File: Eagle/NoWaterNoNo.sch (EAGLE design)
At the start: 14 parts, among them U2 TINY85-20-DIP

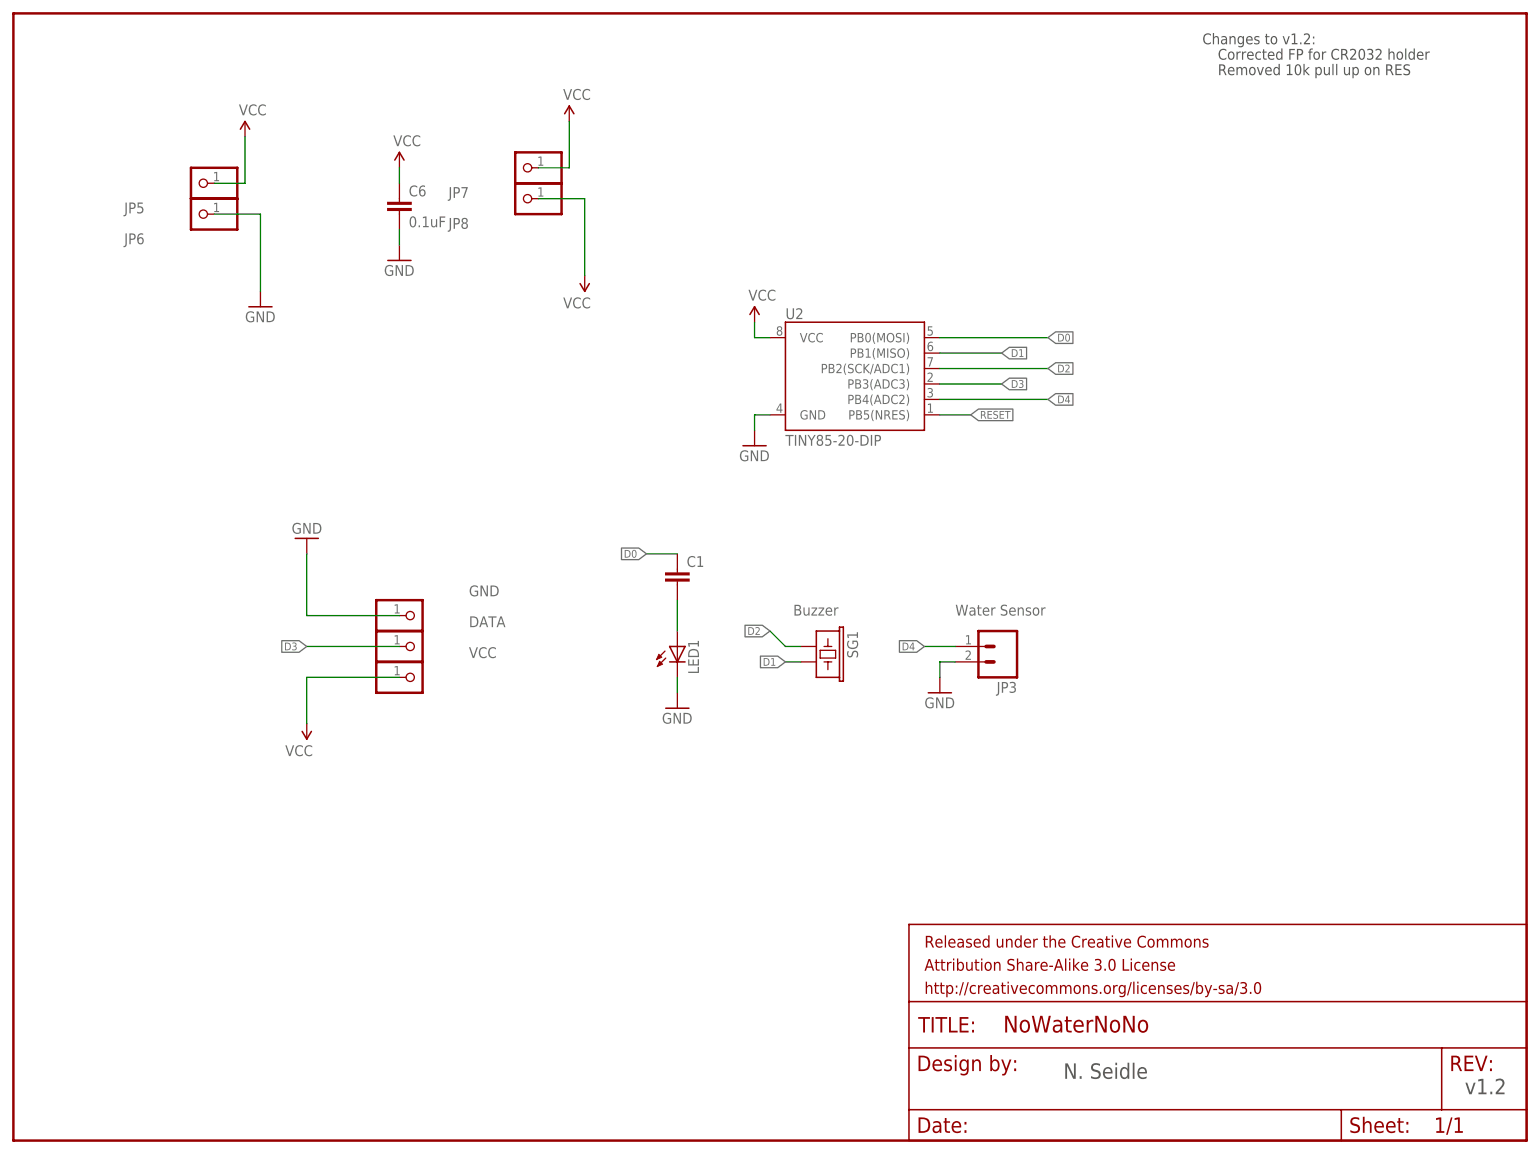
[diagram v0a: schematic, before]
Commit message: Eagle: BRD and SCH files from test branch were more up to date than master.
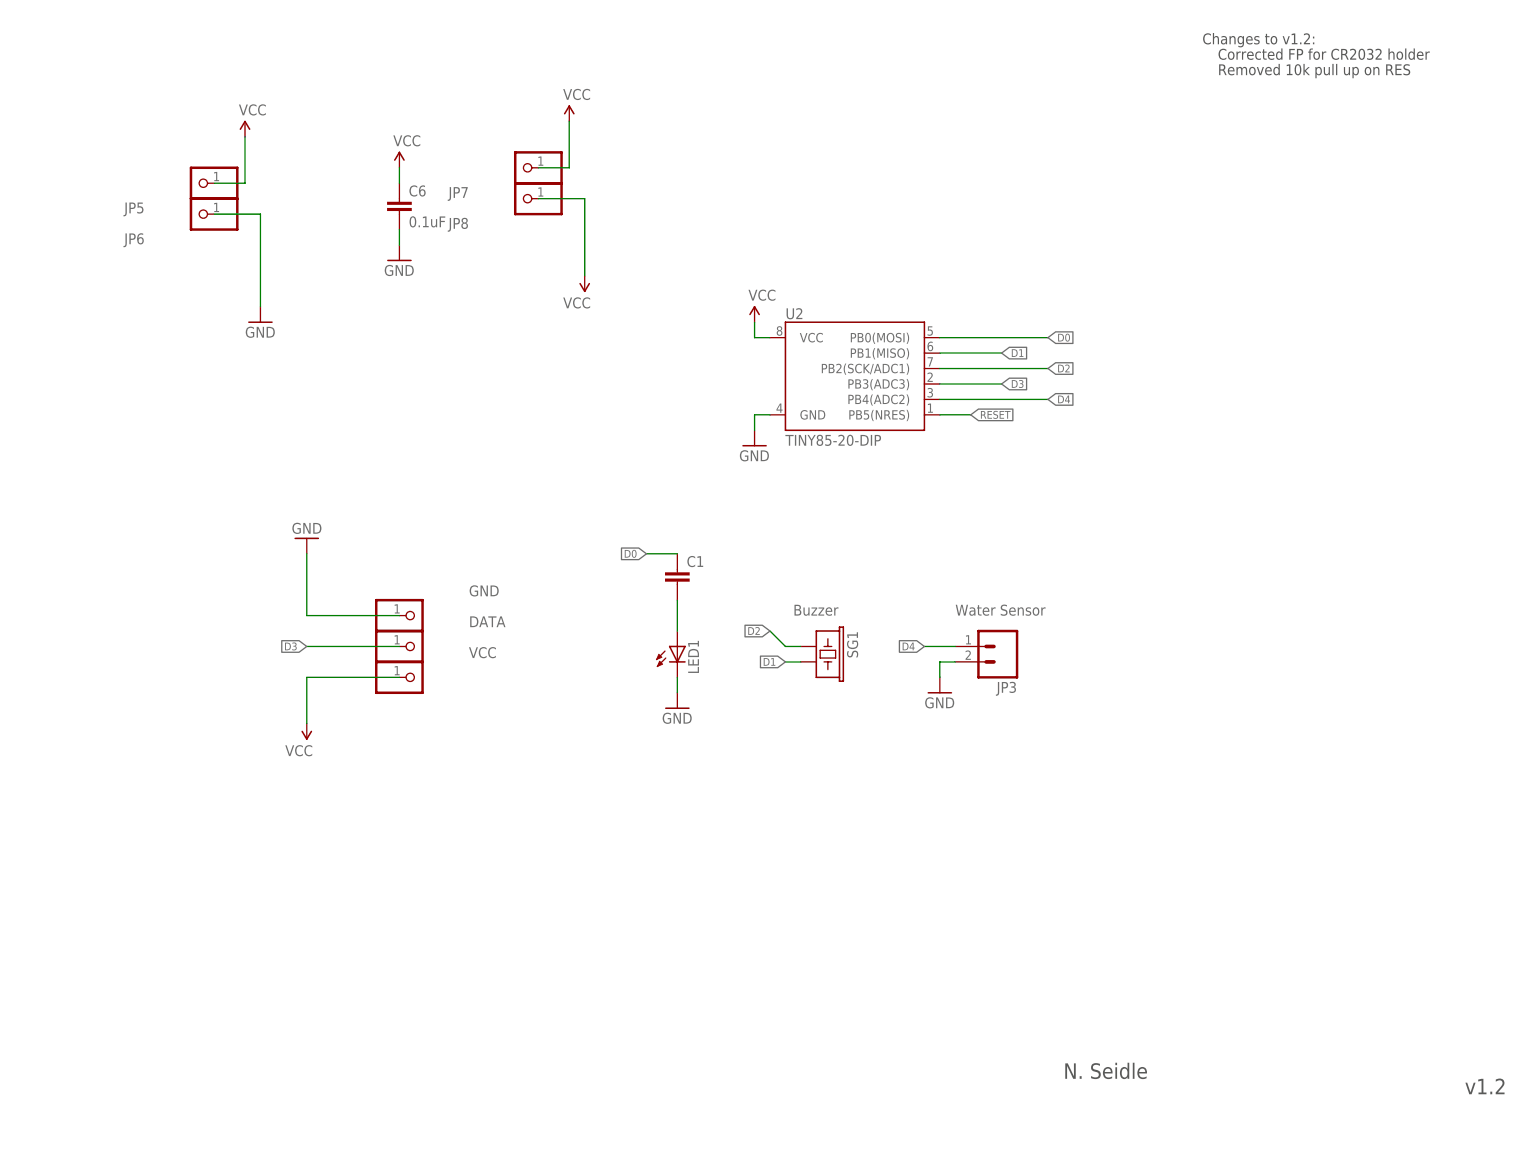
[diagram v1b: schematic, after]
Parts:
- removed FRAME2: FRAME-LETTER, SparkFun-Aesthetics:FRAME-LETTER
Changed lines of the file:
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@@
 <?xml version="1.0" encoding="utf-8"?>
 <!DOCTYPE eagle SYSTEM "eagle.dtd">
-<eagle version="6.4">
+<eagle version="6.5.0">
 <drawing>
 <settings>
@@
 <part name="GND8" library="SparkFun" deviceset="GND" device=""/>
 <part name="GND9" library="SparkFun" deviceset="GND" device=""/>
-<part name="FRAME2" library="SparkFun-Aesthetics" deviceset="FRAME-LETTER" device=""/>
 <part name="GND" library="pinhead" deviceset="PINHD-1X1" device=""/>
 <part name="DATA" library="pinhead" deviceset="PINHD-1X1" device=""/>
@@
 <instance part="GND23" gate="1" x="63.5" y="144.78"/>
 <instance part="P+3" gate="1" x="63.5" y="160.02"/>
-<instance part="GND7" gate="1" x="40.64" y="137.16"/>
+<instance part="GND7" gate="1" x="40.64" y="134.62"/>
 <instance part="P+2" gate="1" x="38.1" y="165.1"/>
 <instance part="U2" gate="G$1" x="139.7" y="124.46" smashed="yes">
@@
 <instance part="GND8" gate="1" x="109.22" y="71.12"/>
 <instance part="GND9" gate="1" x="152.4" y="73.66"/>
-<instance part="FRAME2" gate="G$1" x="0" y="0"/>
-<instance part="FRAME2" gate="G$2" x="147.32" y="0"/>
 <instance part="GND" gate="G$1" x="66.04" y="86.36" smashed="yes">
 <attribute name="NAME" x="74.93" y="89.535" size="1.778" layer="95"/>
@@
 <pinref part="JP6" gate="G$1" pin="1"/>
 <wire x1="33.02" y1="152.4" x2="40.64" y2="152.4" width="0.1524" layer="91"/>
-<wire x1="40.64" y1="152.4" x2="40.64" y2="139.7" width="0.1524" layer="91"/>
+<wire x1="40.64" y1="152.4" x2="40.64" y2="137.16" width="0.1524" layer="91"/>
 </segment>
 <segment>
